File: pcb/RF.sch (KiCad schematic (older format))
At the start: 50 parts, among them P401 CONN_01X02, P402 CONN_01X02, U401 MAX2750, U402 MGA-635P8, U403 HHM1520, U404 MGA-635P8, U405 LT5560, U406 PD2328J, U407 WA04P

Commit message: board ready to route
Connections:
- net MIXER_IN: now also U403.1 (50_PORT)
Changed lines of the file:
@@
 	3750 6300 3750 6350
 Wire Wire Line
-	1450 6750 1550 6750
+	1050 6750 1550 6750
 Wire Wire Line
 	1500 7200 1500 7150
@@
 Connection ~ 1500 6200
 Wire Wire Line
-	1150 6750 1050 6750
-Wire Wire Line
 	6150 6150 6350 6150

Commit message: added PDF schematic
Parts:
- U402, U404: footprint Housings_DFN_QFN:DFN-8-1EP_2x2mm_Pitch0.5mm -> wbraun_smd:8-QFN-2x2
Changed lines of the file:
@@
 F 0 "U402" H 1950 4850 60  0000 C CNN
 F 1 "MGA-635P8" H 2200 4150 60  0000 C CNN
-F 2 "Housings_DFN_QFN:DFN-8-1EP_2x2mm_Pitch0.5mm" H 2200 4500 60  0001 C CNN
+F 2 "wbraun_smd:8-QFN-2x2" H 2200 4500 60  0001 C CNN
 F 3 "" H 2200 4500 60  0001 C CNN
 	1    2200 4500
@@
 F 0 "U404" H 4350 2550 60  0000 C CNN
 F 1 "MGA-635P8" H 4600 1850 60  0000 C CNN
-F 2 "Housings_DFN_QFN:DFN-8-1EP_2x2mm_Pitch0.5mm" H 4600 2200 60  0001 C CNN
+F 2 "wbraun_smd:8-QFN-2x2" H 4600 2200 60  0001 C CNN
 F 3 "" H 4600 2200 60  0001 C CNN
 	1    4600 2200

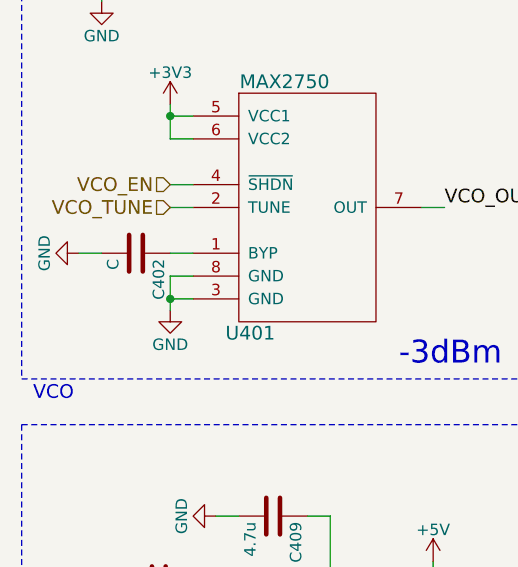
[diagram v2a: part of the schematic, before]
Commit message: new uc and added AGC. Sent off to fab
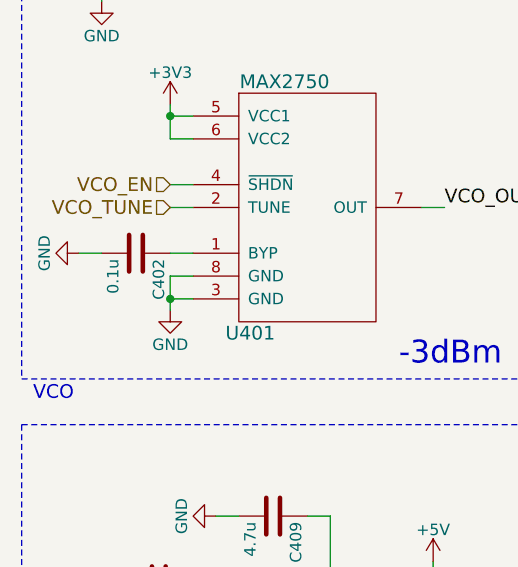
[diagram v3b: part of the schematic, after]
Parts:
- C402: value C -> 0.1u
- P401, P402: footprint wbraun_smd:SMA-Edge -> wbraun_smd:SMA-Edge-short
- U401: footprint Housings_SSOP:MSOP-8_3x3mm_Pitch0.65mm -> wbraun_smd:MSOP-8_3x3mm
- U405: footprint Housings_DFN_QFN:DFN-8-1EP_3x3mm_Pitch0.5mm -> wbraun_smd:DFN-8-3x3
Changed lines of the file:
@@
 F 0 "U405" H 5400 6750 60  0000 C CNN
 F 1 "LT5560" H 5500 5650 60  0000 C CNN
-F 2 "Housings_DFN_QFN:DFN-8-1EP_3x3mm_Pitch0.5mm" H 6000 5500 60  0001 C CNN
+F 2 "wbraun_smd:DFN-8-3x3" H 6000 5500 60  0001 C CNN
 F 3 "" H 6000 5500 60  0001 C CNN
 	1    5650 6200
@@
 F 0 "U401" H 1550 1600 60  0000 C CNN
 F 1 "MAX2750" H 1700 2700 60  0000 C CNN
-F 2 "Housings_SSOP:MSOP-8_3x3mm_Pitch0.65mm" H 2200 1550 60  0001 C CNN
+F 2 "wbraun_smd:MSOP-8_3x3mm" H 2200 1550 60  0001 C CNN
 F 3 "" H 2200 1550 60  0001 C CNN
 	1    1800 2150
@@
 $EndComp
 $Comp
-L GND #PWR043
+L GND #PWR411
 U 1 1 58AA10B9
 P 1600 4800
-F 0 "#PWR043" H 1600 4550 50  0001 C CNN
+F 0 "#PWR411" H 1600 4550 50  0001 C CNN
 F 1 "GND" H 1600 4650 50  0000 C CNN
 F 2 "" H 1600 4800 50  0000 C CNN
@@
 $EndComp
 $Comp
-L GND #PWR044
+L GND #PWR404
 U 1 1 58AA10EF
 P 900 3800
-F 0 "#PWR044" H 900 3550 50  0001 C CNN
+F 0 "#PWR404" H 900 3550 50  0001 C CNN
 F 1 "GND" H 900 3650 50  0000 C CNN
 F 2 "" H 900 3800 50  0000 C CNN
@@
 $EndComp
 $Comp
-L GND #PWR045
+L GND #PWR407
 U 1 1 58AA1125
 P 1400 3500
-F 0 "#PWR045" H 1400 3250 50  0001 C CNN
+F 0 "#PWR407" H 1400 3250 50  0001 C CNN
 F 1 "GND" H 1400 3350 50  0000 C CNN
 F 2 "" H 1400 3500 50  0000 C CNN
@@
 $EndComp
 $Comp
-L GND #PWR046
+L GND #PWR419
 U 1 1 58AA115B
 P 3400 4000
-F 0 "#PWR046" H 3400 3750 50  0001 C CNN
+F 0 "#PWR419" H 3400 3750 50  0001 C CNN
 F 1 "GND" H 3400 3850 50  0000 C CNN
 F 2 "" H 3400 4000 50  0000 C CNN
@@
 $EndComp
 $Comp
-L GND #PWR047
+L GND #PWR418
 U 1 1 58AA1191
 P 3400 3500
-F 0 "#PWR047" H 3400 3250 50  0001 C CNN
+F 0 "#PWR418" H 3400 3250 50  0001 C CNN
 F 1 "GND" H 3400 3350 50  0000 C CNN
 F 2 "" H 3400 3500 50  0000 C CNN
@@
 $EndComp
 $Comp
-L +5V #PWR048
+L +5V #PWR413
 U 1 1 58AA11C7
 P 2900 3400
-F 0 "#PWR048" H 2900 3250 50  0001 C CNN
+F 0 "#PWR413" H 2900 3250 50  0001 C CNN
 F 1 "+5V" H 2900 3540 50  0000 C CNN
 F 2 "" H 2900 3400 50  0000 C CNN
@@
 $EndComp
 $Comp
-L +5V #PWR049
+L +5V #PWR412
 U 1 1 58AA11FD
 P 2350 3700
-F 0 "#PWR049" H 2350 3550 50  0001 C CNN
+F 0 "#PWR412" H 2350 3550 50  0001 C CNN
 F 1 "+5V" H 2350 3840 50  0000 C CNN
 F 2 "" H 2350 3700 50  0000 C CNN
@@
 $EndComp
 $Comp
-L GND #PWR050
+L GND #PWR417
 U 1 1 58AA2399
 P 3350 6950
-F 0 "#PWR050" H 3350 6700 50  0001 C CNN
+F 0 "#PWR417" H 3350 6700 50  0001 C CNN
 F 1 "GND" H 3350 6800 50  0000 C CNN
 F 2 "" H 3350 6950 50  0000 C CNN
@@
 $EndComp
 $Comp
-L GND #PWR051
+L GND #PWR420
 U 1 1 58AA2A6C
 P 3750 6350
-F 0 "#PWR051" H 3750 6100 50  0001 C CNN
+F 0 "#PWR420" H 3750 6100 50  0001 C CNN
 F 1 "GND" H 3750 6200 50  0000 C CNN
 F 2 "" H 3750 6350 50  0000 C CNN
@@
 $EndComp
 $Comp
-L GND #PWR052
+L GND #PWR414
 U 1 1 58AA2AB8
 P 3250 6350
-F 0 "#PWR052" H 3250 6100 50  0001 C CNN
+F 0 "#PWR414" H 3250 6100 50  0001 C CNN
 F 1 "GND" H 3250 6200 50  0000 C CNN
 F 2 "" H 3250 6350 50  0000 C CNN
@@
 $EndComp
 $Comp
-L GND #PWR053
+L GND #PWR410
 U 1 1 58AA2B04
 P 1500 7200
-F 0 "#PWR053" H 1500 6950 50  0001 C CNN
+F 0 "#PWR410" H 1500 6950 50  0001 C CNN
 F 1 "GND" H 1500 7050 50  0000 C CNN
 F 2 "" H 1500 7200 50  0000 C CNN
@@
 $EndComp
 $Comp
-L GND #PWR054
+L GND #PWR416
 U 1 1 58AA32CA
 P 3350 5600
-F 0 "#PWR054" H 3350 5350 50  0001 C CNN
+F 0 "#PWR416" H 3350 5350 50  0001 C CNN
 F 1 "GND" H 3350 5450 50  0000 C CNN
 F 2 "" H 3350 5600 50  0000 C CNN
@@
 MIXER_IN+
 $Comp
-L GND #PWR055
+L GND #PWR425
 U 1 1 58AA3ACB
 P 5050 6700
-F 0 "#PWR055" H 5050 6450 50  0001 C CNN
+F 0 "#PWR425" H 5050 6450 50  0001 C CNN
 F 1 "GND" H 5050 6550 50  0000 C CNN
 F 2 "" H 5050 6700 50  0000 C CNN
@@
 $EndComp
 $Comp
-L GND #PWR056
+L GND #PWR409
 U 1 1 58AA3E57
 P 1500 6250
-F 0 "#PWR056" H 1500 6000 50  0001 C CNN
+F 0 "#PWR409" H 1500 6000 50  0001 C CNN
 F 1 "GND" H 1500 6100 50  0000 C CNN
 F 2 "" H 1500 6250 50  0000 C CNN
@@
 $EndComp
 $Comp
-L +5V #PWR057
+L +5V #PWR408
 U 1 1 58AA4282
 P 1500 5750
-F 0 "#PWR057" H 1500 5600 50  0001 C CNN
+F 0 "#PWR408" H 1500 5600 50  0001 C CNN
 F 1 "+5V" H 1500 5890 50  0000 C CNN
 F 2 "" H 1500 5750 50  0000 C CNN
@@
 $EndComp
 $Comp
-L +5V #PWR058
+L +5V #PWR424
 U 1 1 58AA42F1
 P 4950 6400
-F 0 "#PWR058" H 4950 6250 50  0001 C CNN
+F 0 "#PWR424" H 4950 6250 50  0001 C CNN
 F 1 "+5V" H 4950 6540 50  0000 C CNN
 F 2 "" H 4950 6400 50  0000 C CNN
@@
 $EndComp
 $Comp
-L +5V #PWR059
+L +5V #PWR432
 U 1 1 58AA4D6B
 P 6300 6650
-F 0 "#PWR059" H 6300 6500 50  0001 C CNN
+F 0 "#PWR432" H 6300 6500 50  0001 C CNN
 F 1 "+5V" H 6300 6790 50  0000 C CNN
 F 2 "" H 6300 6650 50  0000 C CNN
@@
 $EndComp
 $Comp
-L +5V #PWR060
+L +5V #PWR431
 U 1 1 58AA4DBF
 P 6300 5750
-F 0 "#PWR060" H 6300 5600 50  0001 C CNN
+F 0 "#PWR431" H 6300 5600 50  0001 C CNN
 F 1 "+5V" H 6300 5890 50  0000 C CNN
 F 2 "" H 6300 5750 50  0000 C CNN
@@
 $EndComp
 $Comp
-L GND #PWR061
+L GND #PWR422
 U 1 1 58AA62C7
 P 4000 2500
-F 0 "#PWR061" H 4000 2250 50  0001 C CNN
+F 0 "#PWR422" H 4000 2250 50  0001 C CNN
 F 1 "GND" H 4000 2350 50  0000 C CNN
 F 2 "" H 4000 2500 50  0000 C CNN
@@
 $EndComp
 $Comp
-L GND #PWR062
+L GND #PWR415
 U 1 1 58AA62CD
 P 3300 1500
-F 0 "#PWR062" H 3300 1250 50  0001 C CNN
+F 0 "#PWR415" H 3300 1250 50  0001 C CNN
 F 1 "GND" H 3300 1350 50  0000 C CNN
 F 2 "" H 3300 1500 50  0000 C CNN
@@
 $EndComp
 $Comp
-L GND #PWR063
+L GND #PWR421
 U 1 1 58AA62D3
 P 3800 1200
-F 0 "#PWR063" H 3800 950 50  0001 C CNN
+F 0 "#PWR421" H 3800 950 50  0001 C CNN
 F 1 "GND" H 3800 1050 50  0000 C CNN
 F 2 "" H 3800 1200 50  0000 C CNN
@@
 $EndComp
 $Comp
-L GND #PWR064
+L GND #PWR428
 U 1 1 58AA62D9
 P 5800 1700
-F 0 "#PWR064" H 5800 1450 50  0001 C CNN
+F 0 "#PWR428" H 5800 1450 50  0001 C CNN
 F 1 "GND" H 5800 1550 50  0000 C CNN
 F 2 "" H 5800 1700 50  0000 C CNN
@@
 $EndComp
 $Comp
-L GND #PWR065
+L GND #PWR427
 U 1 1 58AA62DF
 P 5800 1200
-F 0 "#PWR065" H 5800 950 50  0001 C CNN
+F 0 "#PWR427" H 5800 950 50  0001 C CNN
 F 1 "GND" H 5800 1050 50  0000 C CNN
 F 2 "" H 5800 1200 50  0000 C CNN
@@
 $EndComp
 $Comp
-L +5V #PWR066
+L +5V #PWR426
 U 1 1 58AA62E5
 P 5300 1100
-F 0 "#PWR066" H 5300 950 50  0001 C CNN
+F 0 "#PWR426" H 5300 950 50  0001 C CNN
 F 1 "+5V" H 5300 1240 50  0000 C CNN
 F 2 "" H 5300 1100 50  0000 C CNN
@@
 $EndComp
 $Comp
-L +5V #PWR067
+L +5V #PWR423
 U 1 1 58AA62EB
 P 4750 1400
-F 0 "#PWR067" H 4750 1250 50  0001 C CNN
+F 0 "#PWR423" H 4750 1250 50  0001 C CNN
 F 1 "+5V" H 4750 1540 50  0000 C CNN
 F 2 "" H 4750 1400 50  0000 C CNN
@@
 P 1050 2350
 F 0 "C402" H 1075 2450 50  0000 L CNN
-F 1 "C" H 1075 2250 50  0000 L CNN
+F 1 "0.1u" H 1075 2250 50  0000 L CNN
 F 2 "Capacitors_SMD:C_0603" H 1088 2200 50  0001 C CNN
 F 3 "" H 1050 2350 50  0000 C CNN
@@
 $EndComp
 $Comp
-L +3V3 #PWR068
+L +3V3 #PWR402
 U 1 1 58AA6803
 P 900 750
-F 0 "#PWR068" H 900 600 50  0001 C CNN
+F 0 "#PWR402" H 900 600 50  0001 C CNN
 F 1 "+3V3" H 900 890 50  0000 C CNN
 F 2 "" H 900 750 50  0000 C CNN
@@
 $EndComp
 $Comp
-L +3V3 #PWR069
+L +3V3 #PWR405
 U 1 1 58AA6877
 P 1200 1700
-F 0 "#PWR069" H 1200 1550 50  0001 C CNN
+F 0 "#PWR405" H 1200 1550 50  0001 C CNN
 F 1 "+3V3" H 1200 1840 50  0000 C CNN
 F 2 "" H 1200 1700 50  0000 C CNN
@@
 $EndComp
 $Comp
-L GND #PWR070
+L GND #PWR403
 U 1 1 58AA68EB
 P 900 1250
-F 0 "#PWR070" H 900 1000 50  0001 C CNN
+F 0 "#PWR403" H 900 1000 50  0001 C CNN
 F 1 "GND" H 900 1100 50  0000 C CNN
 F 2 "" H 900 1250 50  0000 C CNN
@@
 $EndComp
 $Comp
-L GND #PWR071
+L GND #PWR406
 U 1 1 58AA695F
 P 1200 2600
-F 0 "#PWR071" H 1200 2350 50  0001 C CNN
+F 0 "#PWR406" H 1200 2350 50  0001 C CNN
 F 1 "GND" H 1200 2450 50  0000 C CNN
 F 2 "" H 1200 2600 50  0000 C CNN
@@
 $EndComp
 $Comp
-L GND #PWR072
+L GND #PWR401
 U 1 1 58AA69D3
 P 800 2350
-F 0 "#PWR072" H 800 2100 50  0001 C CNN
+F 0 "#PWR401" H 800 2100 50  0001 C CNN
 F 1 "GND" H 800 2200 50  0000 C CNN
 F 2 "" H 800 2350 50  0000 C CNN
@@
 VCO_OUT
 $Comp
-L GND #PWR073
+L GND #PWR433
 U 1 1 58AA8C7D
 P 7100 1800
-F 0 "#PWR073" H 7100 1550 50  0001 C CNN
+F 0 "#PWR433" H 7100 1550 50  0001 C CNN
 F 1 "GND" H 7100 1650 50  0000 C CNN
 F 2 "" H 7100 1800 50  0000 C CNN
@@
 $EndComp
 $Comp
-L GND #PWR074
+L GND #PWR434
 U 1 1 58AA97AD
 P 8600 1950
-F 0 "#PWR074" H 8600 1700 50  0001 C CNN
+F 0 "#PWR434" H 8600 1700 50  0001 C CNN
 F 1 "GND" H 8600 1800 50  0000 C CNN
 F 2 "" H 8600 1950 50  0000 C CNN
@@
 $EndComp
 $Comp
-L GND #PWR075
+L GND #PWR435
 U 1 1 58AA9851
 P 9600 2000
-F 0 "#PWR075" H 9600 1750 50  0001 C CNN
+F 0 "#PWR435" H 9600 1750 50  0001 C CNN
 F 1 "GND" H 9600 1850 50  0000 C CNN
 F 2 "" H 9600 2000 50  0000 C CNN
@@
 F 0 "P402" H 6350 3650 50  0000 C CNN
 F 1 "CONN_01X02" V 6450 3500 50  0000 C CNN
-F 2 "wbraun_smd:SMA-Edge" H 6350 3500 50  0001 C CNN
+F 2 "wbraun_smd:SMA-Edge-short" H 6350 3500 50  0001 C CNN
 F 3 "" H 6350 3500 50  0000 C CNN
 	1    6350 3500
@@
 F 0 "P401" H 6300 4550 50  0000 C CNN
 F 1 "CONN_01X02" V 6400 4400 50  0000 C CNN
-F 2 "wbraun_smd:SMA-Edge" H 6300 4400 50  0001 C CNN
+F 2 "wbraun_smd:SMA-Edge-short" H 6300 4400 50  0001 C CNN
 F 3 "" H 6300 4400 50  0000 C CNN
 	1    6300 4400
@@
 $EndComp
 $Comp
-L GND #PWR076
+L GND #PWR430
 U 1 1 58AAC543
 P 6100 3650
-F 0 "#PWR076" H 6100 3400 50  0001 C CNN
+F 0 "#PWR430" H 6100 3400 50  0001 C CNN
 F 1 "GND" H 6100 3500 50  0000 C CNN
 F 2 "" H 6100 3650 50  0000 C CNN
@@
 $EndComp
 $Comp
-L GND #PWR077
+L GND #PWR429
 U 1 1 58AAC5BB
 P 6050 4550
-F 0 "#PWR077" H 6050 4300 50  0001 C CNN
+F 0 "#PWR429" H 6050 4300 50  0001 C CNN
 F 1 "GND" H 6050 4400 50  0000 C CNN
 F 2 "" H 6050 4550 50  0000 C CNN
